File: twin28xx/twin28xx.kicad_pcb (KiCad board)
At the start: 4 copper layers, 76.9 x 36.9 mm, 212 parts, among them J1 XY-SH1_0-3A61, J10 Conn_01x03, J11 XY-SH1_0-6A51, J12 XY-SH1_0-6A51, J13 Conn_01x04, J2 TYPE-C-31-M-12, J4 DB125-2_54-2P-GN__mirror, J5 XY-SH1_0-4A61, J6 DB125-2_54-2P-GN, J7 XY-SH1_0-3A61, J8 XY-SH1_0-3A61, J9 Conn_01x03, Q1 AO3401A, SW1 SKSGPAE010, SW2 SKSGPAE010, U1 BK22C07-4DP/2-0_4V(800), U10 SRV05-4A, U11 CA-IF1044VD-Q1, U12 ACT1210D-101-2P-TL00, U13 PESD2CAN, U14 DRV8316CRRGFR, U15 DRV8316CRRGFR, U16 MT6701QT, U17 SRV05-4A, U18 MT6701QT, U19 SRV05-4A, U2 BK22C07-4DP/2-0_4V(800), U3 FMMT620TA, U4 WSD4066DN, U5 SMF30A_C19077518, U6 SRV05-4A, U7 STM32G473RBTx, U8 TPD1E10B06DPYR, U9 XC6206P332MR, X1 X322512MSB4SI

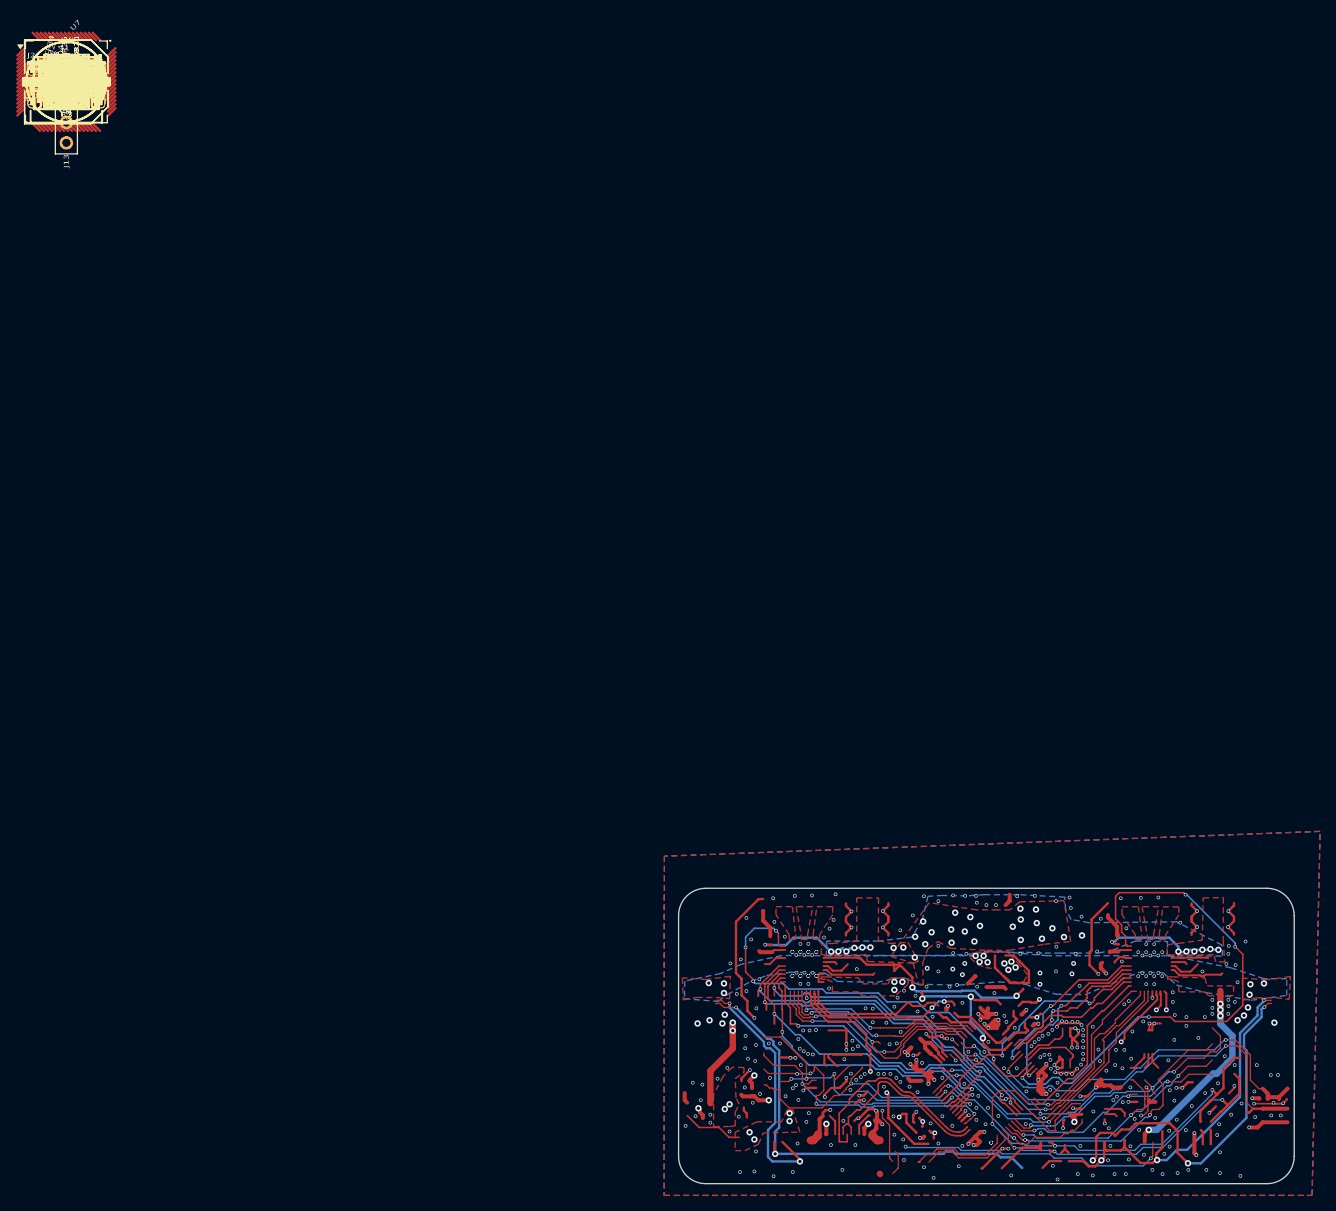
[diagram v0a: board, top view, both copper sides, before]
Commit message: swap bulk caps to VHXC hybrid, add second DRV8316 stage, relayout PCB
- motor_driver: replace 5x GRM21BR61H106KE43L bulk caps with 3x
  VHXC0581V101MVCG hybrid caps; add U14 (DRV8316CRRGFR), L1
  (PRS3015-470MT), R29, and associated decoupling (C38-44, C52, C61-66)
- PCB: relayout/reroute for the new parts
- refs: add Ymin VHXC and Chuanghui SV101M datasheets
- tools: add splitbank_sim.py power-delivery sim
- analysis: track manifest.json (outputs stay ignored)

Co-Authored-By: Claude Opus 5 (1M context) <noreply@anthropic.com>
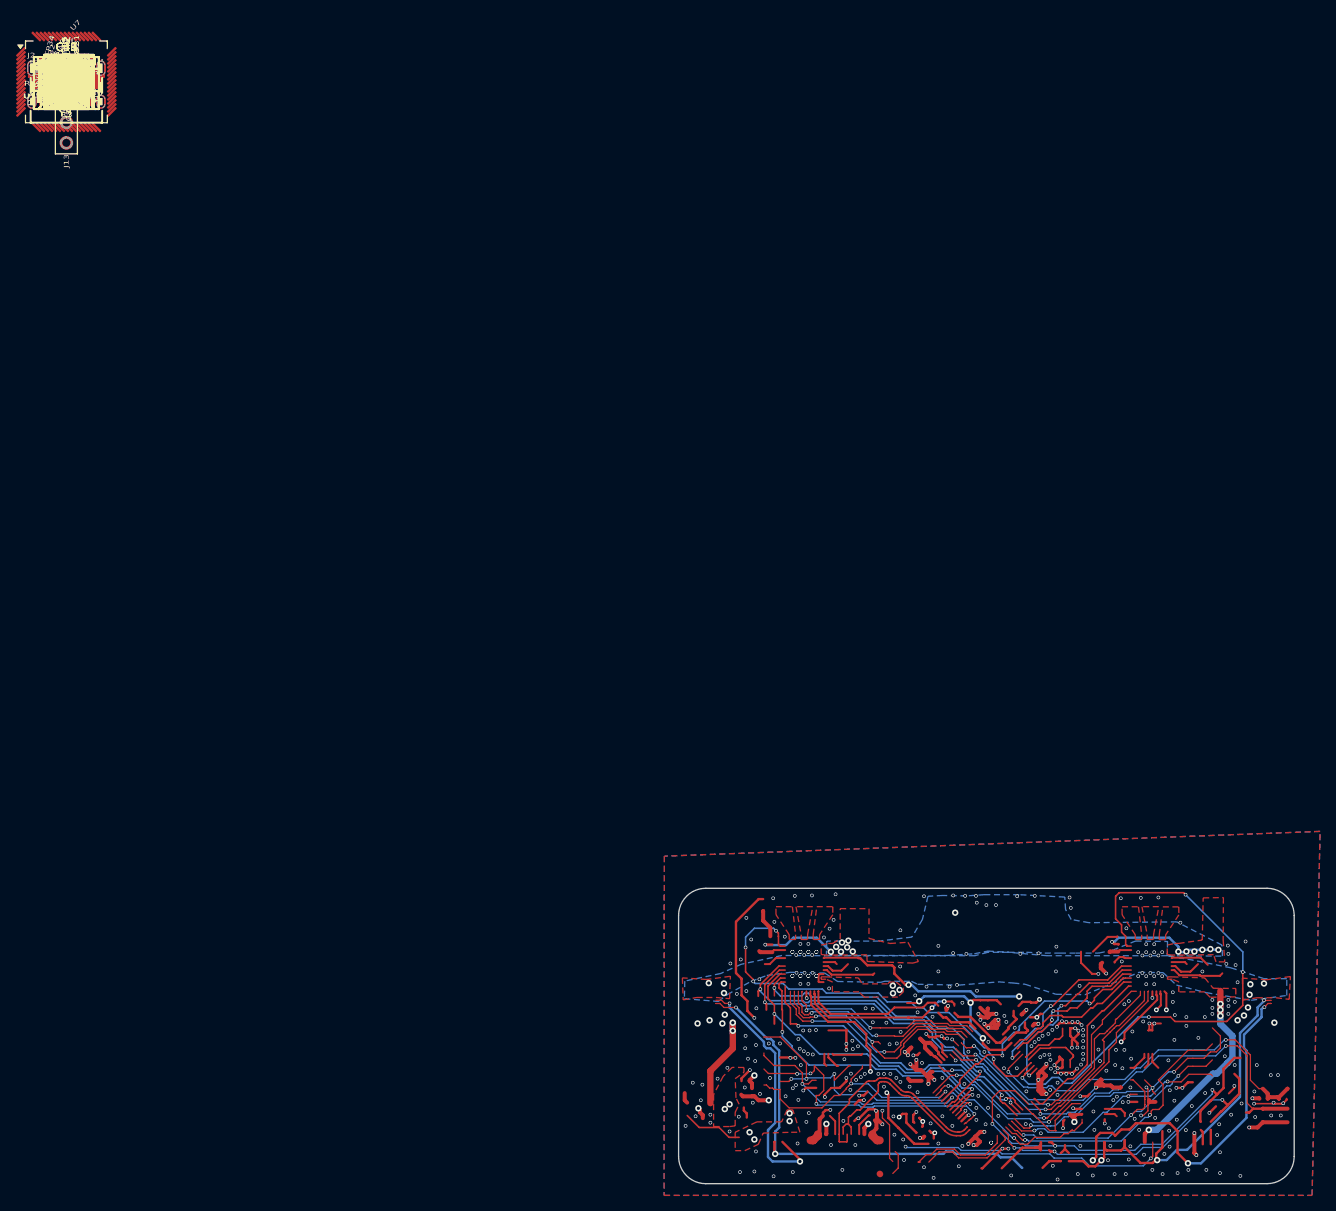
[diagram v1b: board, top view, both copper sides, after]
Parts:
- removed C44, C58: 50PX330MEFC10X16, Capacitor_THT__C:CAP-TH_BD10.0-P5.00-D1.0-FD
- removed C52, C53, C54, C55, C56: GRM21BR61H106KE43L, Capacitor_SMD:C_0805_2012Metric
- removed C57: EEEFT1H331GP, Capacitor_SMD__C:CAP-SMD_BD10.0-L10.3-W10.3-LS11.0-R-RD
- C38, C39, C40, C41, C42: value GRM21BR61H106KE43L -> VHXC0581V101MVCG; footprint Capacitor_SMD:C_0805_2012Metric -> Capacitor_SMD:CP_Elec_6.3x5.8
- C43: value EEEFT1H331GP -> VHXC0581V101MVCG; footprint Capacitor_SMD__C:CAP-SMD_BD10.0-L10.3-W10.3-LS11.0-R-RD -> Capacitor_SMD:CP_Elec_6.3x5.8
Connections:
- C38 pad 1: GND -> VCC
- C38 pad 2: VCC -> GND
- C39 pad 1: GND -> VCC
- C39 pad 2: VCC -> GND
- C40 pad 1: GND -> VCC
- C40 pad 2: VCC -> GND
- C41 pad 1: GND -> VCC
- C41 pad 2: VCC -> GND
- C42 pad 1: GND -> VCC
- C42 pad 2: VCC -> GND
- C43 pad 1: GND -> VCC
- C43 pad 2: VCC -> GND
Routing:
- net GND: track 98.5 -> 77.9 mm, vias 385 -> 369
- net Net-(U3-C): track 11.8 -> 0.00 mm
- net +3.3V: track 123.0 -> 116.8 mm
- net VCC: track 31.9 -> 26.4 mm, vias 40 -> 16
- net /VCP: track 30.3 -> 27.0 mm
- net Net-(D1-A): track 2.52 -> 0.00 mm
- net /BUCK: track 38.5 -> 40.6 mm
- net Net-(LED1-K): track 1.51 -> 0.00 mm
- net Net-(U3-B): track 1.38 -> 0.00 mm
- net /VSENS: track 22.0 -> 22.8 mm
- net Net-(LED4-K): track 3.15 -> 3.86 mm
- net +BATT: vias 22 -> 6
